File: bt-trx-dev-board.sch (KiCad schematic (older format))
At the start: 12 parts, among them J1 RJ45, J2 PTT_BUTTON, J3 AudioJack2, J4 ENAPLE_PTT_PULLUP, J5 PTT_SELECT, U1 SILabs_WT32i

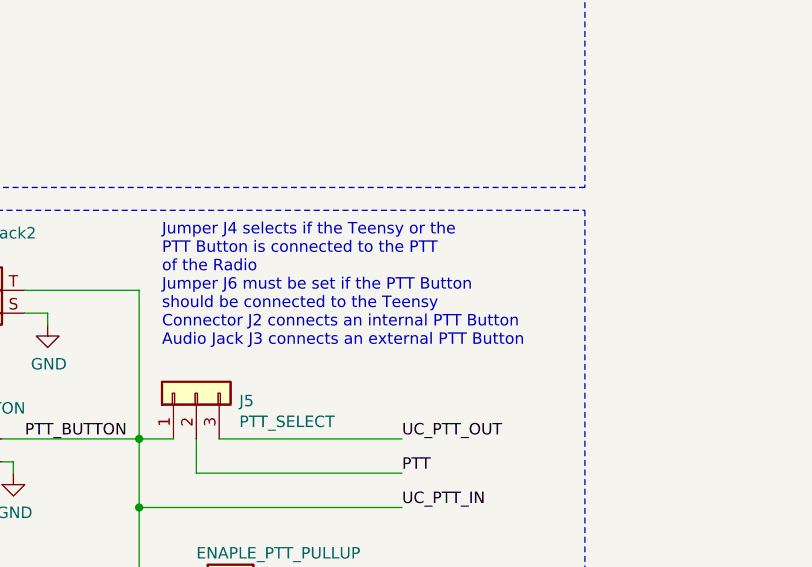
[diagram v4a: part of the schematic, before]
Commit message: Fix some comments
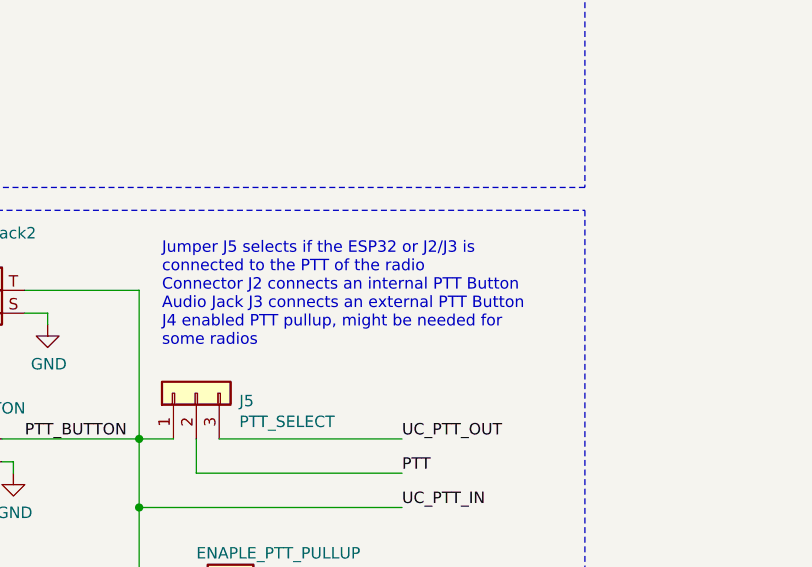
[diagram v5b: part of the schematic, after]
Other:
- note added: "Jumper J5 selects if the ESP32 or J2/J3 is\nconnected to the PTT of the radio\nConnector J2 connects an internal PTT Button\nAudio Jack J3 connects an external PTT Button\nJ4 enabled PTT pullup, might be needed for\nsome radios"
- note removed: "Jumper J4 selects if the Teensy or the\nPTT Button is connected to the PTT\nof the Radio\nJumper J6 must be set if the PTT Button\nshould be connected to the Teensy\nConnector J2 connects an internal PTT Button\nAudio Jack J3 connects an external PTT Button"
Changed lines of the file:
@@
 EESchema Schematic File Version 4
 LIBS:bt-trx-dev-board-cache
-EELAYER 26 0
+EELAYER 29 0
 EELAYER END
 $Descr A4 11693 8268
@@
 UC_PTT_IN
 Text Notes 4450 5400 0    50   ~ 0
-Jumper J4 selects if the Teensy or the\nPTT Button is connected to the PTT\nof the Radio\nJumper J6 must be set if the PTT Button\nshould be connected to the Teensy\nConnector J2 connects an internal PTT Button\nAudio Jack J3 connects an external PTT Button
+Jumper J5 selects if the ESP32 or J2/J3 is\nconnected to the PTT of the radio\nConnector J2 connects an internal PTT Button\nAudio Jack J3 connects an external PTT Button\nJ4 enabled PTT pullup, might be needed for\nsome radios
 Wire Notes Line
 	3350 6950 6300 6950
